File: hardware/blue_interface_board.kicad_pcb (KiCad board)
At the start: 4 copper layers, 70 x 70 mm, 130 parts, among them J1 arm connector, J10 I2C, J2 USB_B_Micro, J3 ESTOP, J4 PWR, J5 Conn_ARM_JTAG_SWD_10, J6 logic-side RS485 debug/expans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, J7 FAN, J8 power-side RS485 debug/expans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, J9 DEBUG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

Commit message: Updating to new files and minor resistor fix
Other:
- net class Default removed
- board text removed: "12V"

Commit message: Adding ERD resistors to layout.
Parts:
- added R38: 10, Resistor_SMD:R_0603_1608Metric, F.Cu at (100.8, 108.1)
- added R39: 2, Resistor_SMD:R_0603_1608Metric, F.Cu at (103.8, 108.1)
- C31: value 100n -> 1u
- R14: value 15m -> 5m
- R15: value 140k -> 240k
- R16: value 21k -> 13.3k
- R17: value 21k -> 300k
- moved C27 1.42 mm to (101.5, 110.0)
- moved Q1 1.33 mm to (101.0, 112.9)
- moved R9 0.79 mm to (104.3, 112.3)
- moved D3 0.77 mm to (107.0, 110.7)
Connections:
- U6 pad 3: Net-(Q2-Pad2) -> Net-(R38-Pad2)
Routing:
- net Net-(R38-Pad2): track 0.00 -> 19.6 mm, vias 0 -> 2
- net Net-(Q2-Pad2): track 24.3 -> 12.1 mm, vias 2 -> 0
- net /Power/VIN: track 33.0 -> 36.4 mm
- net /Power/GATE: track 14.5 -> 13.1 mm
- net Net-(C27-Pad1): track 5.79 -> 6.81 mm
- net GND: track 110.0 -> 109.3 mm

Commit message: Removing external resistor divider.
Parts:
- removed R38: 10, Resistor_SMD:R_0603_1608Metric
- removed R39: 2, Resistor_SMD:R_0603_1608Metric
- C31: value 1u -> 100n
- R14: value 5m -> 15m
- R15: value 240k -> 140k
- R16: value 13.3k -> 21k
- R17: value 300k -> 21k
- moved C27 1.42 mm to (102.0, 108.7)
- moved Q1 1.33 mm to (101.1, 111.6)
- moved R9 0.79 mm to (104.4, 111.5)
- moved D3 0.77 mm to (107.1, 109.9)
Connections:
- U6 pad 3: Net-(R38-Pad2) -> Net-(Q2-Pad2)
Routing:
- net Net-(R38-Pad2): track 19.6 -> 0.00 mm, vias 2 -> 0
- net Net-(Q2-Pad2): track 12.1 -> 24.3 mm, vias 0 -> 2
- net /Power/VIN: track 36.4 -> 33.0 mm
- net /Power/GATE: track 13.1 -> 14.5 mm
- net Net-(C27-Pad1): track 6.81 -> 5.79 mm
- net GND: track 109.3 -> 110.0 mm

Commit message: Updating info from schematic
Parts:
- C31: value 100n -> 47n
- R14: value 15m -> 4m
- R15: value 140k -> 240k
- R16: value 21k -> 13.3k
- R17: value 21k -> 300k

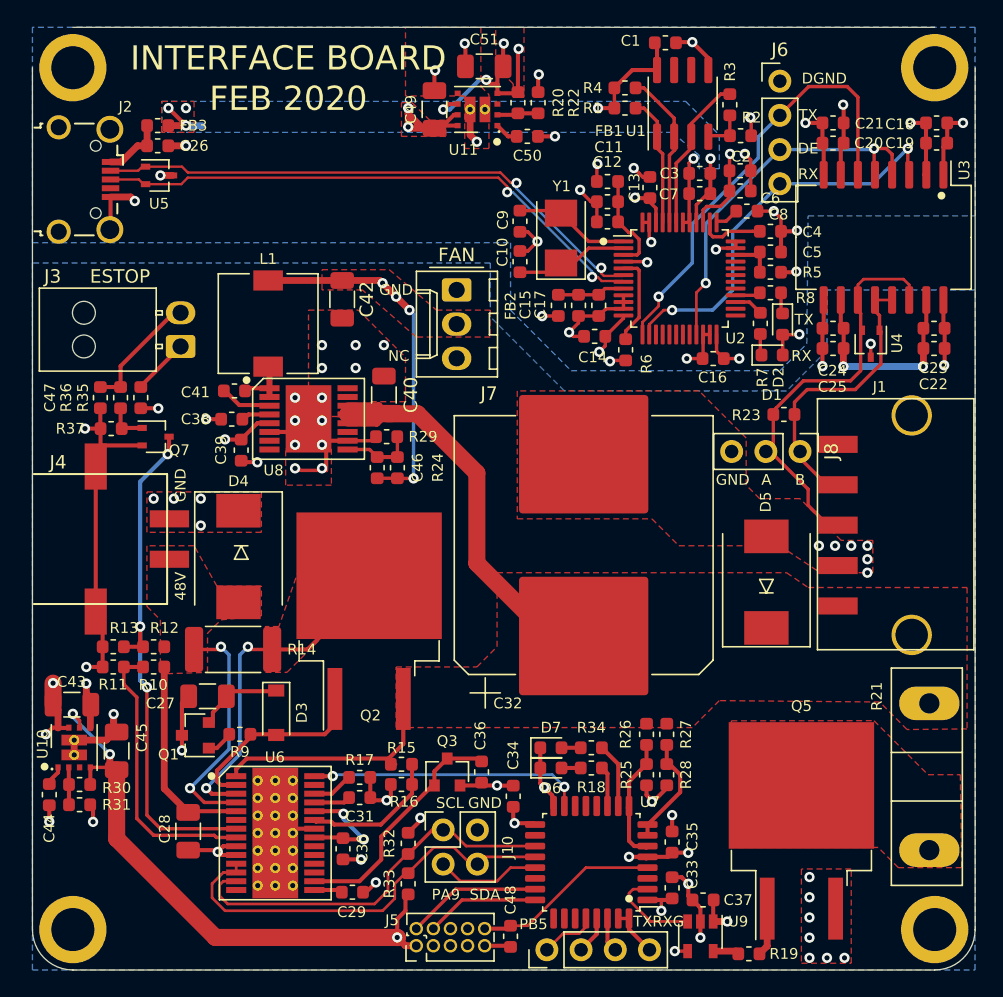
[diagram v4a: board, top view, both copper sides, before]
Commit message: Adding second Power FET
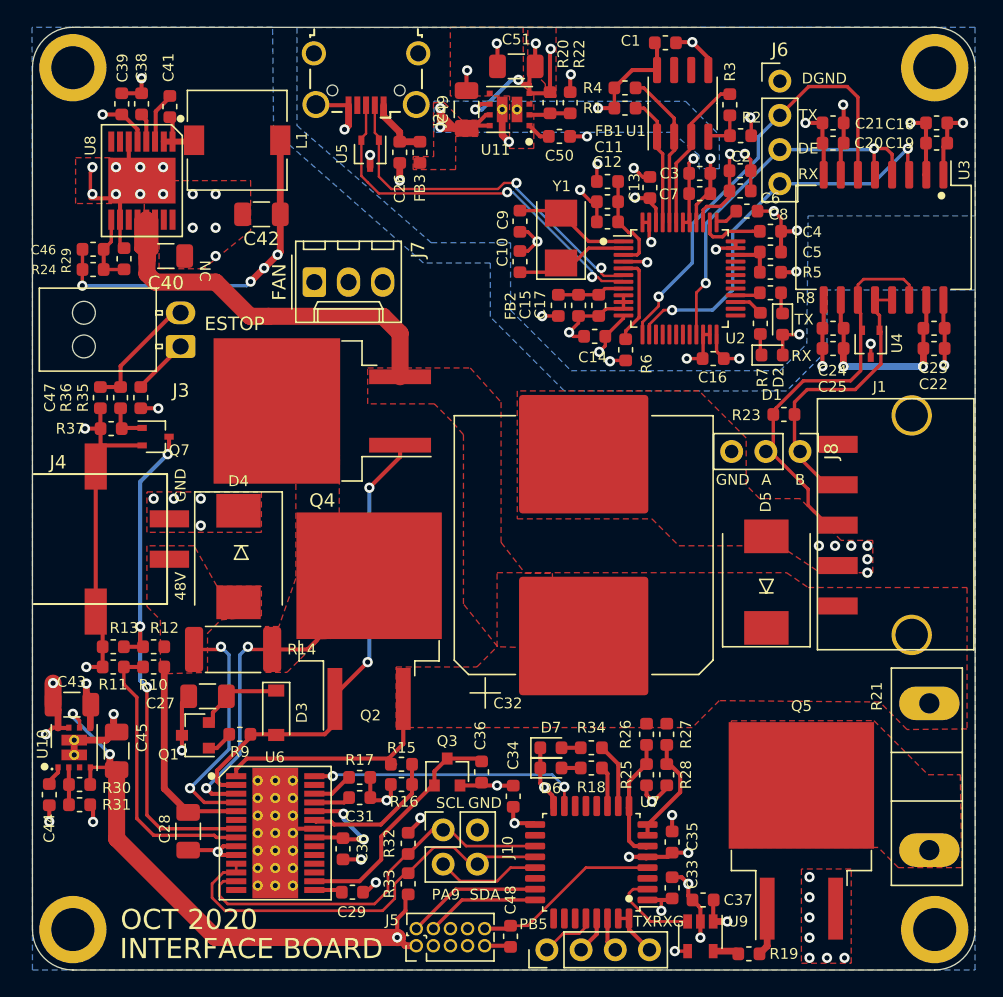
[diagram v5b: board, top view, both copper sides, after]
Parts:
- added Q4: PSMN4R8-100BSEJ, Package_TO_SOT_SMD:TO-263-2, F.Cu at (110.5, 87.5)
- moved C39 27.2 mm to (95.6, 64.7), turned to 90 degrees
- moved R24 27.0 mm to (93.5, 77.0), turned to 0 degrees
- moved C46 26.6 mm to (93.5, 75.5), turned to 0 degrees
- moved C38 24.4 mm to (97.1, 64.7), turned to 90 degrees
- moved R29 23.6 mm to (95.8, 76.2), turned to 90 degrees
- moved J2 22.2 mm to (113.8, 62.9), turned to 180 degrees
- moved C41 21.7 mm to (99.2, 64.9), turned to -90 degrees
- moved U8 21.6 mm to (97.1, 70.4), turned to 180 degrees
- moved FB3 19.6 mm to (117.8, 68.3), turned to -90 degrees
- moved C40 19.2 mm to (98.9, 76.0), turned to 0 degrees
- moved C26 18.0 mm to (116.3, 68.3), turned to -90 degrees
- moved U5 15.8 mm to (114.1, 68.4), turned to -90 degrees
- moved L1 13.8 mm to (104.2, 67.4), turned to 0 degrees
- moved J7 10.6 mm to (109.9, 77.9), turned to 0 degrees
- moved C42 8.71 mm to (106.0, 72.9), turned to 180 degrees
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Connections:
- U6 pad 23: Net-(R15-Pad1) -> Net-(U6-Pad23)
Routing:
- net /Power/GATE: track 14.5 -> 35.3 mm, vias 0 -> 2
- net /Comms/DN: track 42.1 -> 27.5 mm
- net /Comms/DP: track 42.1 -> 28.4 mm
- net Net-(Q2-Pad2): track 24.3 -> 29.9 mm
- net +5V: track 19.7 -> 15.3 mm, vias 6 -> 3
- net /Comms/RS485_B: track 24.3 -> 22.6 mm
- net /Comms/RS485_A: track 34.6 -> 32.8 mm
- net VOUT: track 54.3 -> 55.0 mm
- net GND: track 110.0 -> 110.3 mm, vias 52 -> 51
- removed copper zone on F.Cu, net +12V
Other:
- board text added: "OCT 2020"
- board text removed: "FEB 2020"

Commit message: Revert "Adding second Power FET"
This reverts commit e632f1e0367ea6556d8bc6e08f99c25e5b9f6e16.
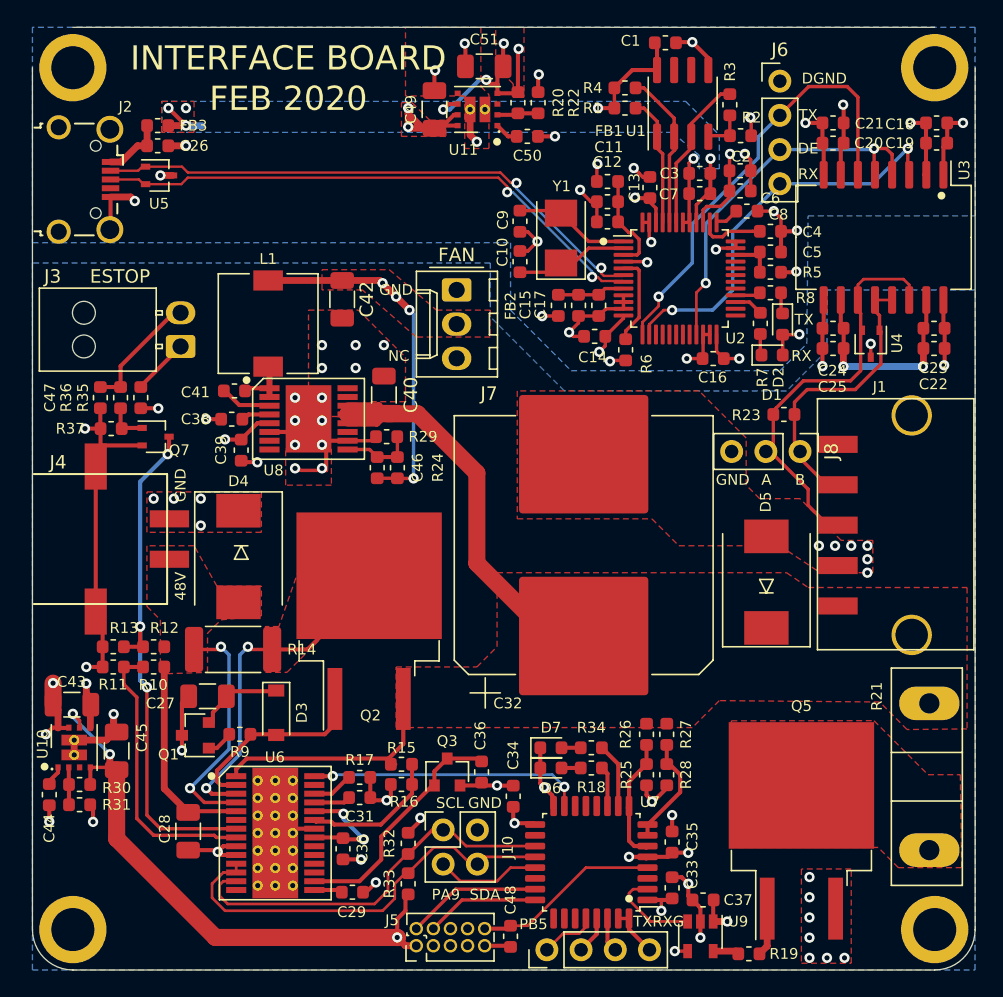
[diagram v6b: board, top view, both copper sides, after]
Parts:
- removed Q4: PSMN4R8-100BSEJ, Package_TO_SOT_SMD:TO-263-2
- moved C39 27.2 mm to (104.5, 90.4), turned to -90 degrees
- moved R24 27.0 mm to (116.1, 91.7), turned to 90 degrees
- moved C46 26.6 mm to (114.6, 91.7), turned to 90 degrees
- moved C38 24.4 mm to (103.8, 88.1), turned to 180 degrees
- moved R29 23.6 mm to (115.3, 89.4), turned to 180 degrees
- moved J2 22.2 mm to (92.9, 70.3), turned to -90 degrees
- moved C41 21.7 mm to (104.0, 86.0), turned to 0 degrees
- moved U8 21.6 mm to (109.5, 88.1), turned to -90 degrees
- moved FB3 19.6 mm to (98.3, 66.3), turned to 0 degrees
- moved C40 19.2 mm to (115.1, 86.3), turned to 90 degrees
- moved C26 18.0 mm to (98.3, 67.8), turned to 0 degrees
- moved U5 15.8 mm to (98.4, 70.0), turned to 0 degrees
- moved L1 13.8 mm to (106.5, 81.0), turned to 90 degrees
- moved J7 10.6 mm to (120.5, 78.5), turned to -90 degrees
- moved C42 8.71 mm to (112.0, 79.2), turned to -90 degrees
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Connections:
- U6 pad 23: Net-(U6-Pad23) -> Net-(R15-Pad1)
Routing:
- net /Power/GATE: track 35.3 -> 14.5 mm, vias 2 -> 0
- net /Comms/DN: track 27.5 -> 42.1 mm
- net /Comms/DP: track 28.4 -> 42.1 mm
- net Net-(Q2-Pad2): track 29.9 -> 24.3 mm
- net +5V: track 15.3 -> 19.7 mm, vias 3 -> 6
- net /Comms/RS485_B: track 22.6 -> 24.3 mm
- net /Comms/RS485_A: track 32.8 -> 34.6 mm
- net VOUT: track 55.0 -> 54.3 mm
- net GND: track 110.3 -> 110.0 mm, vias 51 -> 52
- added copper zone on F.Cu, net +12V
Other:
- board text added: "FEB 2020"
- board text removed: "OCT 2020"

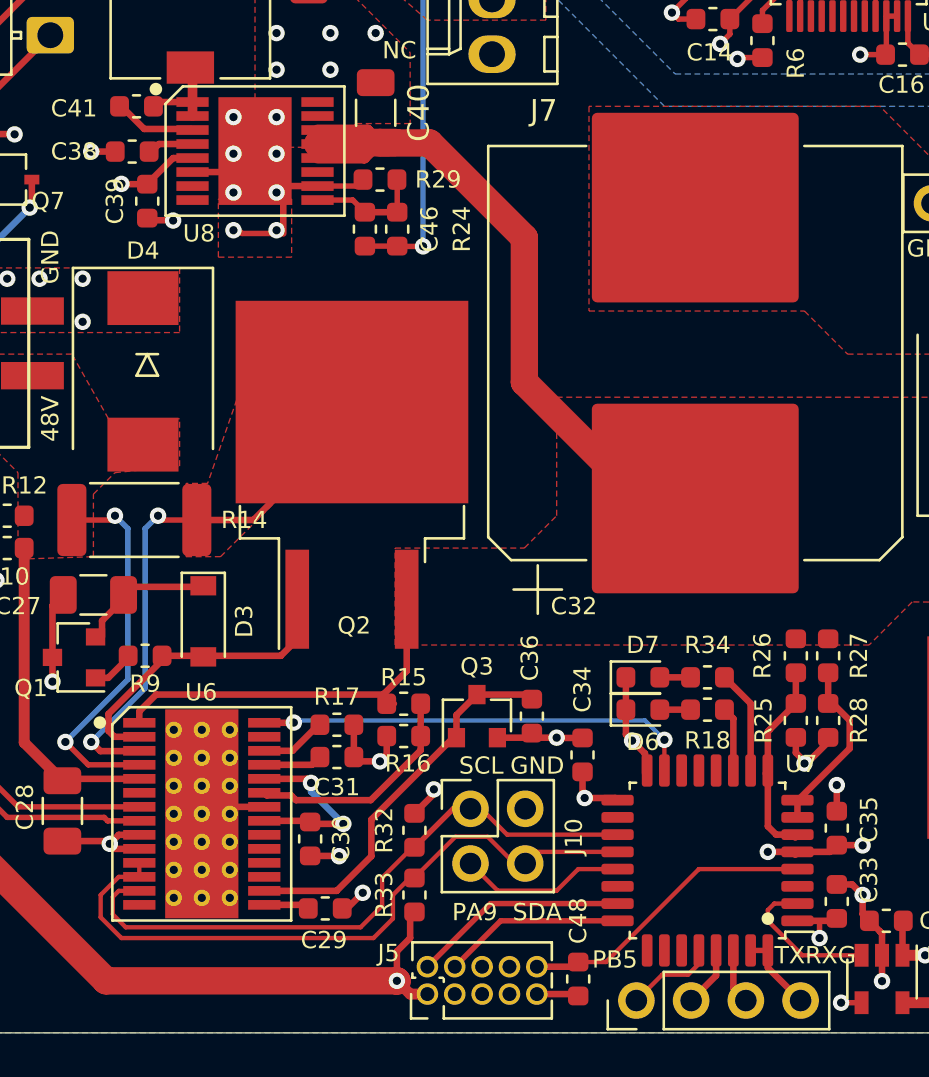
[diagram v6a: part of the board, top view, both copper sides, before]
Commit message: 12V rail supplied off of VIN and Shunt EN switched to a clockable pin.
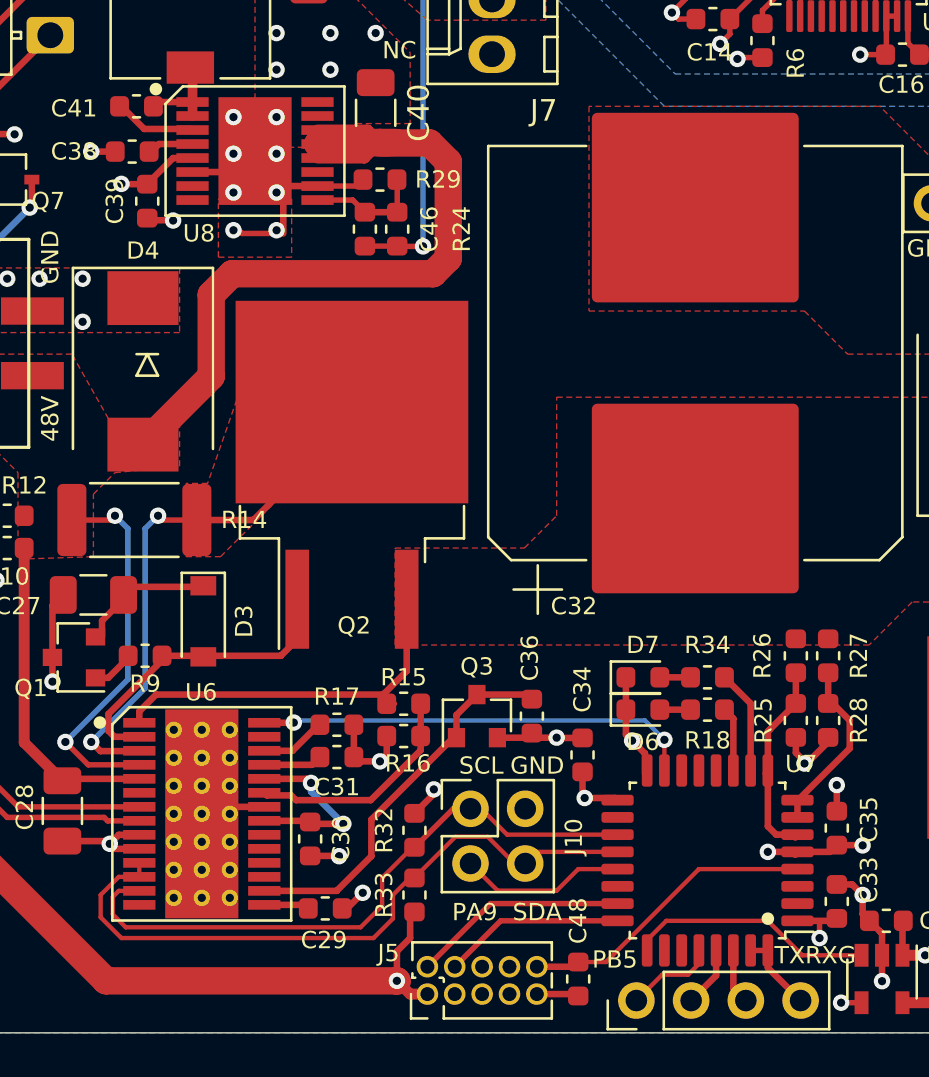
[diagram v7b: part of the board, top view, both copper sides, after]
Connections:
- C40 pad 1: VOUT -> /Power/VIN
- U7 pad 2: /Power/GATE_EN -> Net-(U7-Pad2)
- U7 pad 25: Net-(U7-Pad25) -> /Power/GATE_EN
- U8 pad 12: VOUT -> /Power/VIN
- U8 pad 13: VOUT -> /Power/VIN
- U8 pad 14: VOUT -> /Power/VIN
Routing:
- net /Power/VIN: track 33.0 -> 72.0 mm
- net VOUT: track 54.3 -> 18.0 mm
- net /Power/GATE_EN: track 7.01 -> 11.5 mm
